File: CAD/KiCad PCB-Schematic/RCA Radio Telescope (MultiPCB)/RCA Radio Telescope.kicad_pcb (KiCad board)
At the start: 2 copper layers, 335 x 340.9 mm, 82 parts, among them J1 Screw_Terminal_01x04, J10 FILTER_OUT, J11 ANT, J15 ANT, J16 ANT, J17 ANT, J18 ANT, J19 ANT, J2 9-12V From PoE Splitter, J3 3V Out For LNA, J4 5V Out For Filter Board, J5 5V From SDR, J7 USB_A, J8 USB_A, J9 ANT, Q1 DMP4047LFDE-7, U13 MAX8510EXK30T, U14 TPS62133RGTR, U15 BPF-A1340+, U16 BPF-A1340+, U17 BPF-A355, U3 SKY13588-460LF, U4 SKY13588-460LF, U5 SN74AVC2T244DQER, U6 MIC5365-1.8YC5-TR, U7 MIC5365-3.3YC5-TR

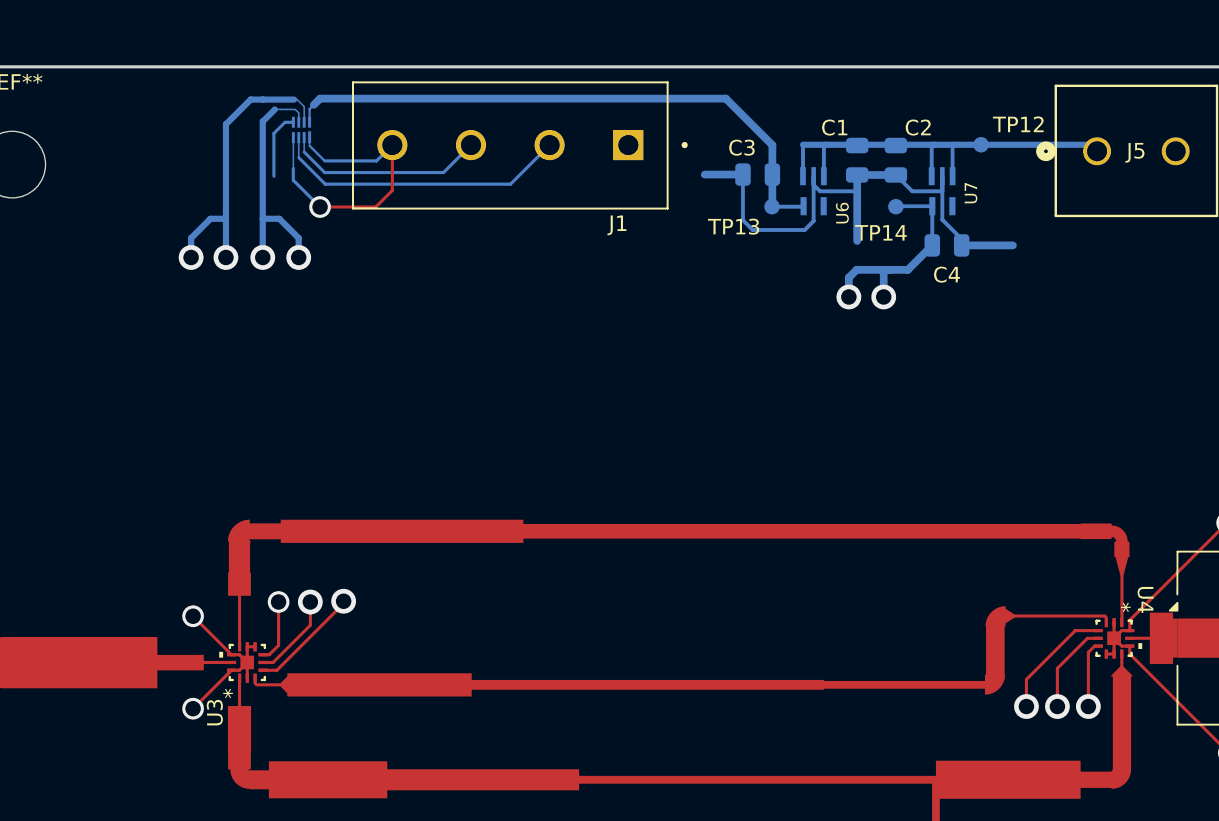
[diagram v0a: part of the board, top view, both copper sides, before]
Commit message: Added Extra Pads and Adjust Layout
Updated RFS PCB to v1.4
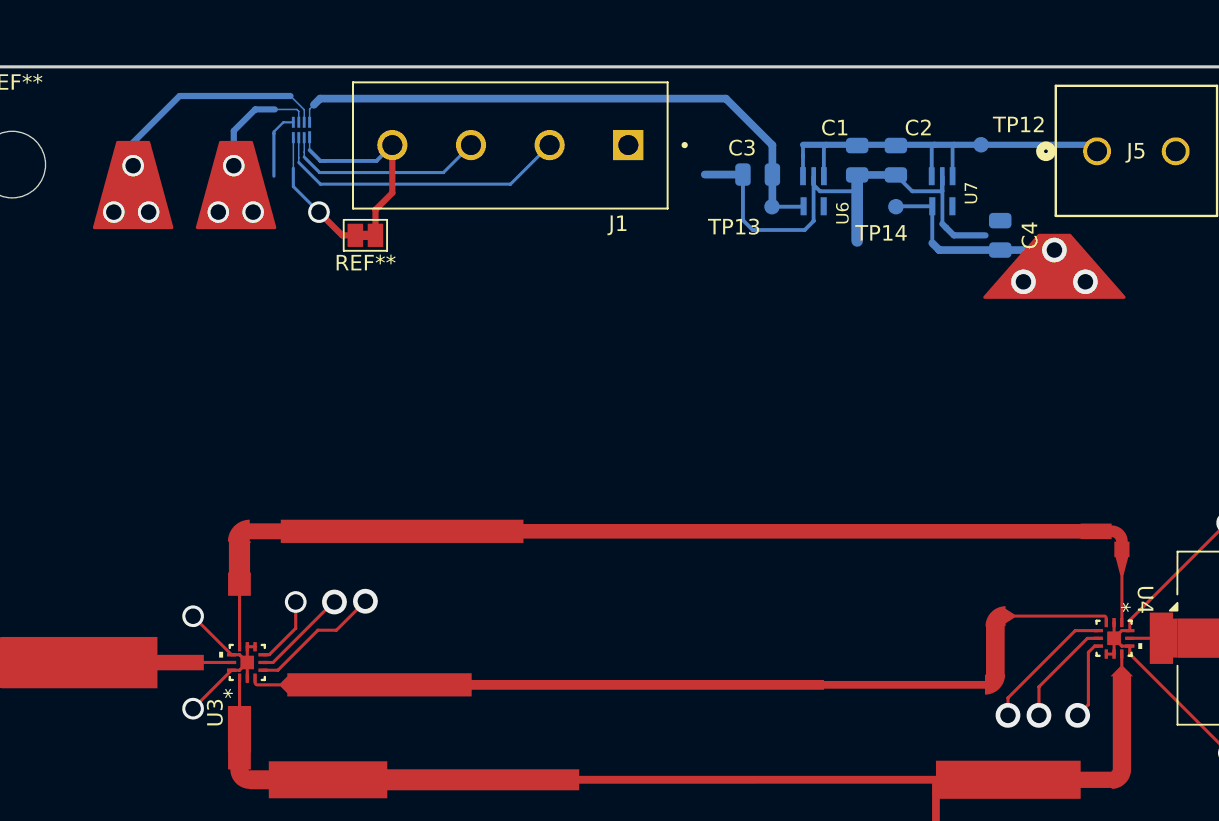
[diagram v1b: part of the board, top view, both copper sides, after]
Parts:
- added REF**: SolderJumper-2_P1.3mm_Bridged_Pad1.0x1.5mm, Jumper:SolderJumper-2_P1.3mm_Bridged_Pad1.0x1.5mm, F.Cu at (259.0, 156.0)
- moved C4 3.50 mm to (300.0, 156.0), turned to -90 degrees
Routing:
- net /RFSwitchFilter/INT_CTRL_V2: track 29.5 -> 22.8 mm, vias 4 -> 5
- net /RFSwitchFilter/INT_CTRL_V1: track 32.6 -> 30.4 mm, vias 4 -> 5
- net /RFS_GND: track 77.8 -> 75.8 mm
- net /RFSwitchFilter/VDD_REF: track 20.0 -> 21.6 mm
- net /RFSwitchFilter/+3V3: track 22.9 -> 22.6 mm, vias 4 -> 5
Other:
- board text added: "RF Switch Filter PCB Rev v1.4 5/6/2025"
- board text removed: "RF Switch Filter PCB Rev v1.3 5/2/2025"

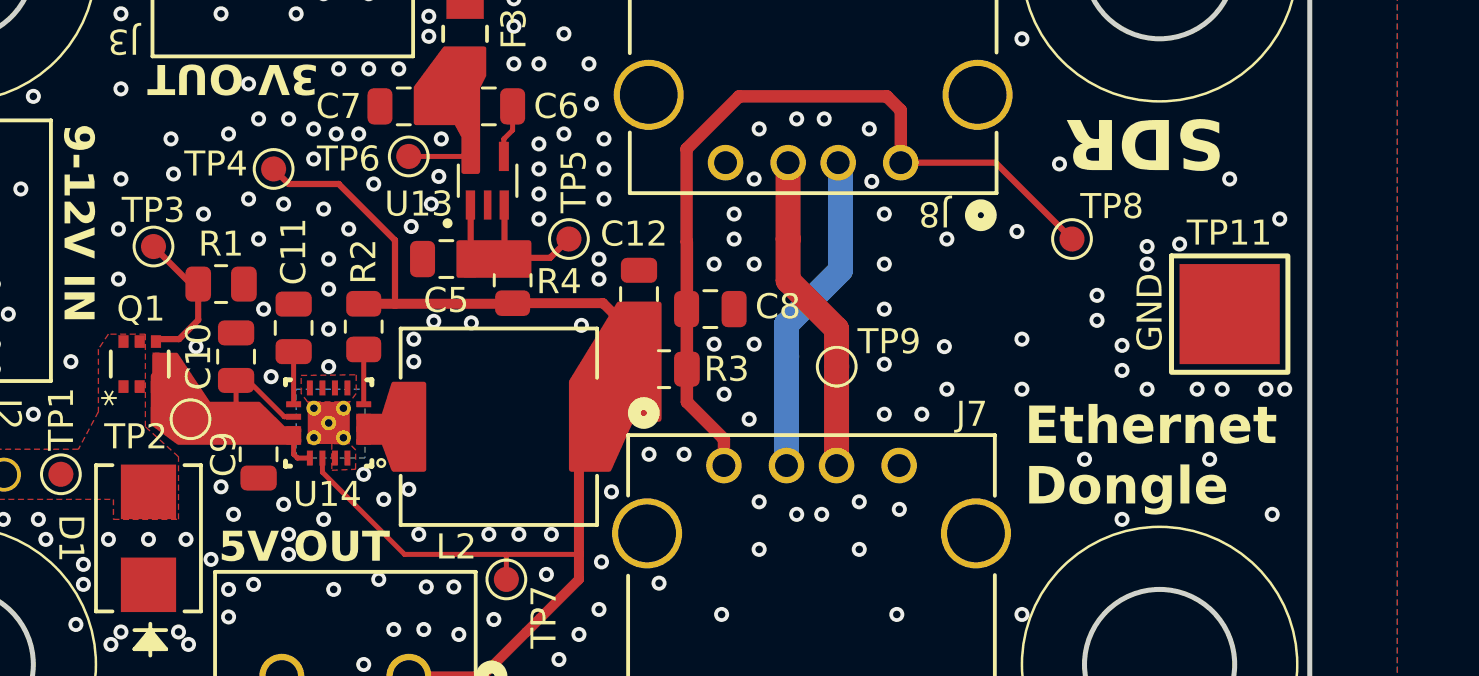
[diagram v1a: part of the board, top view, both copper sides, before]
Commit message: Updated Schematic to Fix USB/PMOS issues and Minor Fixes
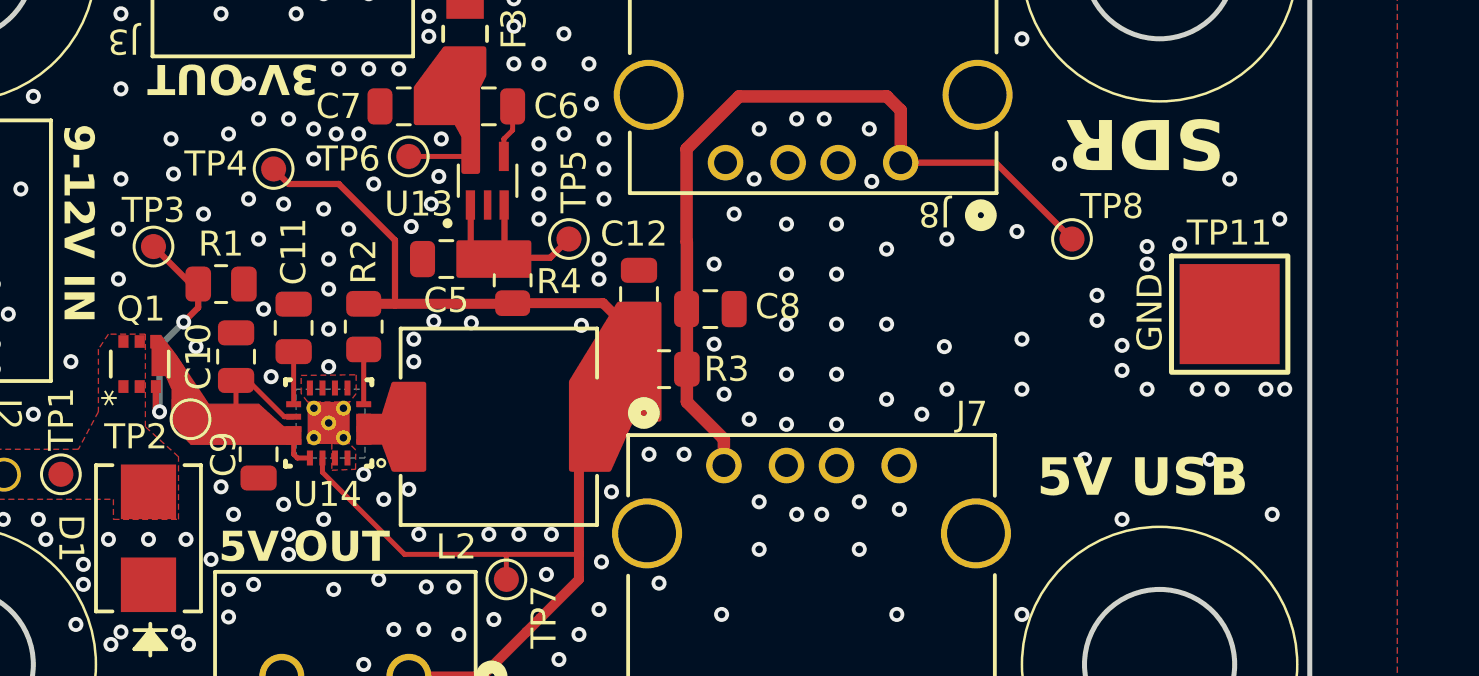
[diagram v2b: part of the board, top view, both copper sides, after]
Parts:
- removed TP10: D-USB, Library:TestPoint_Pad_D1.0mm_Edit
- removed TP9: D+USB, Library:TestPoint_Pad_D1.0mm_Edit
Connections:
- net /PowerDataDistribute/USB_5V_IN renamed Net-(J7-VBUS)
- J7 pad 2: /PowerDataDistribute/USB_D-_IN -> unconnected-(J7-D--Pad2)
- J7 pad 3: /PowerDataDistribute/USB_D+_IN -> unconnected-(J7-D+-Pad3)
- J8 pad 2: /PowerDataDistribute/USB_D-_IN -> unconnected-(J8-D--Pad2)
- J8 pad 3: /PowerDataDistribute/USB_D+_IN -> unconnected-(J8-D+-Pad3)
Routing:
- net /PowerDataDistribute/USB_D-_IN: track 13.0 -> 0.00 mm
- net /PowerDataDistribute/USB_D+_IN: track 12.9 -> 0.00 mm
- net Net-(Q1-G): track 5.75 -> 9.22 mm, vias 0 -> 2
- net /POWERDATA_GND: vias 226 -> 231
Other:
- board text added: "5V USB"
- board text added: "Note: vias are disconnected to have external wires to be solder on"
- board text added: "Power Data Distribute PCB Rev v2.3 6/11/2025"
- board text removed: "Ethernet Dongle"
- board text removed: "Note: Standoffs for RF Switch Filter should be a bit higher to accommodate coax underneath"
- board text removed: "Power Data Distribute PCB Rev v2.2 3/29/2025"
